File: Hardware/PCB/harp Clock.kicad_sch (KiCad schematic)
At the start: 16 parts, among them J2 AudioJack3_Ground_SwitchTR, J3 AudioJack3_Ground_SwitchTR, Q1 AO3401A, U1 74LVC1G157, U3 ADuM1201BR NOT NORMALLY STOCK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

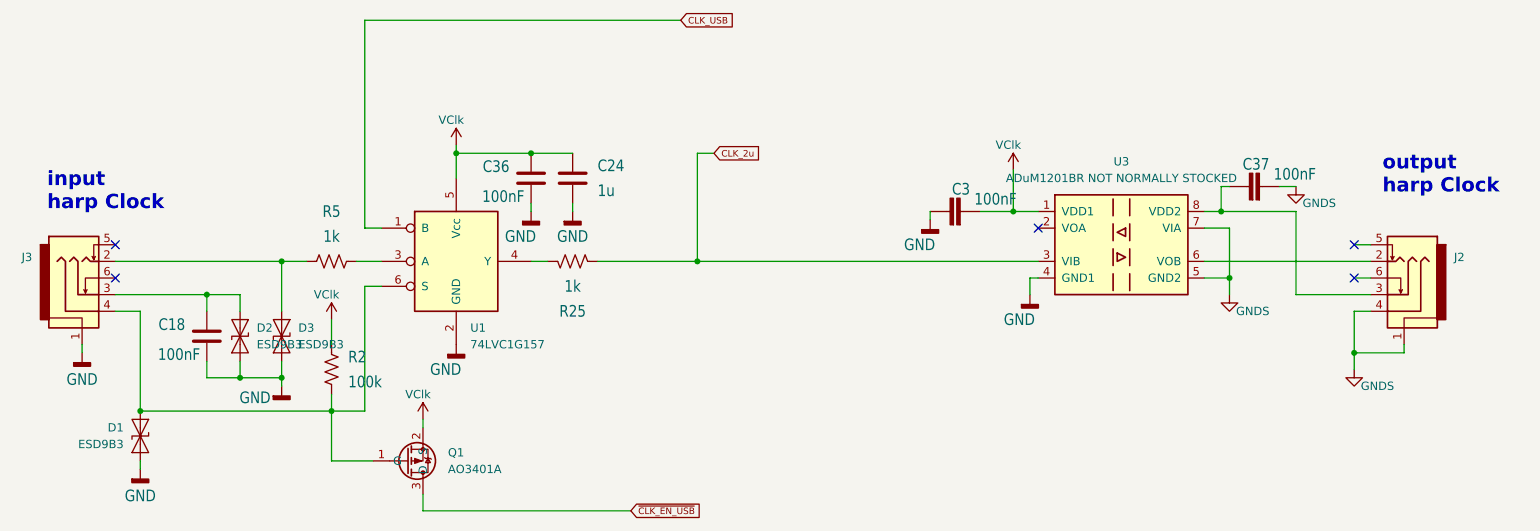
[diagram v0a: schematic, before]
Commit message: FastStepper DRC=0
DRC=0
ainda não revisto com mais ninguém
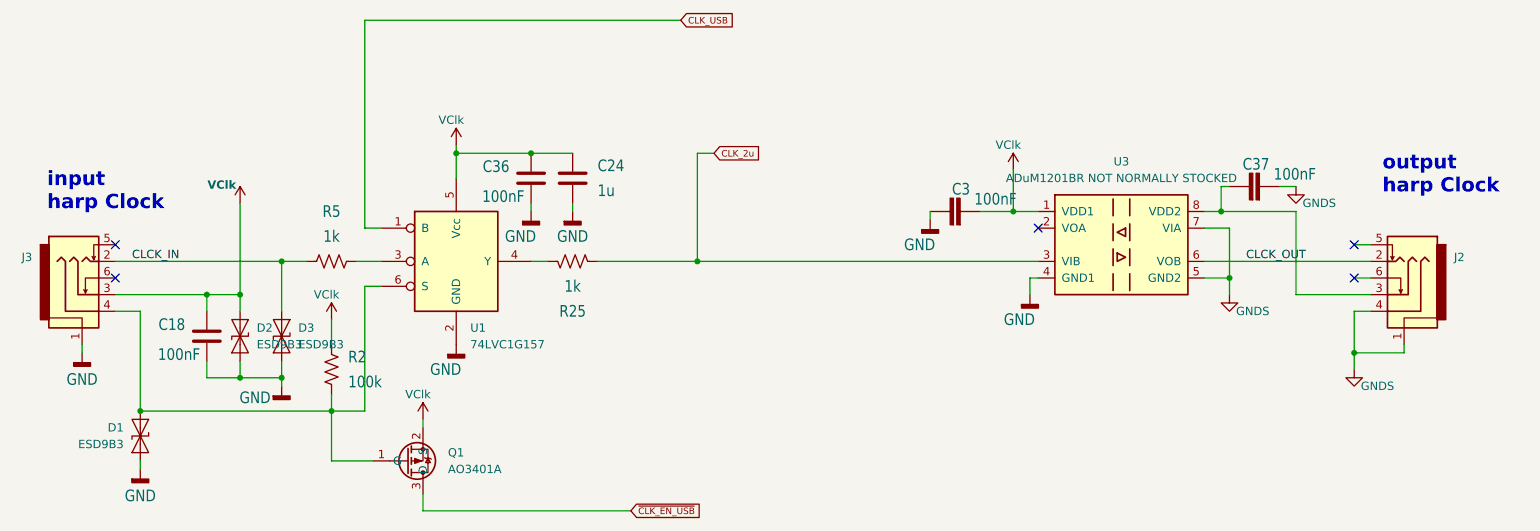
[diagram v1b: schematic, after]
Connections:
- net VClk: now also C18.2, D2.2 (A2), J3.3
- net CLCK_IN: now reaches D3.2 (A2), J3.2, R5.2
- net CLCK_OUT: now reaches J2.2, U3.6 (VOB)
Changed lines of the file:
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@@
+	)
+	(junction
+		(at 68.58 113.03)
+		(diameter 0)
+		(color 0 0 0 0)
 	)
 	(junction
@@
 	(wire
 		(pts
-			(xy 74.93 107.95) (xy 49.53 107.95)
-		)
-		(stroke
-			(width 0)
-			(type default)
-		)
-	)
-	(wire
-		(pts
 			(xy 53.34 139.7) (xy 53.34 138.43)
 		)
@@
 		(pts
 			(xy 90.17 107.95) (xy 86.36 107.95)
+		)
+		(stroke
+			(width 0)
+			(type default)
+		)
+	)
+	(wire
+		(pts
+			(xy 49.53 107.95) (xy 74.93 107.95)
 		)
 		(stroke
@@
 	(wire
 		(pts
+			(xy 68.58 99.06) (xy 68.58 113.03)
+		)
+		(stroke
+			(width 0)
+			(type default)
+		)
+	)
+	(wire
+		(pts
 			(xy 218.44 100.33) (xy 218.44 96.52)
 		)
@@
 			(width 0)
 			(type default)
+		)
+	)
+	(label "CLCK_OUT"
+		(at 222.25 107.95 0)
+		(effects
+			(font
+				(size 1.27 1.27)
+			)
+			(justify left bottom)
+		)
+	)
+	(label "CLCK_IN"
+		(at 52.07 107.95 0)
+		(effects
+			(font
+				(size 1.27 1.27)
+			)
+			(justify left bottom)
 		)
 	)
@@
 					(unit 1)
 				)
+			)
+		)
+	)
+	(symbol
+		(lib_id "FastStepper SymbLib:VClk")
+		(at 68.58 99.06 0)
+		(unit 1)
+		(exclude_from_sim no)
+		(in_bom yes)
+		(on_board yes)
+		(dnp no)
+		(property "Reference" "#PWR017"
+			(at 68.58 102.87 0)
+			(effects
+				(font
+					(size 1.27 1.27)
+				)
+				(hide yes)
+			)
+		)
+		(property "Value" "VClk"
+			(at 65.786 96.266 0)
+			(effects
+				(font
+					(size 1.27 1.27)
+					(thickness 0.254)
+					(bold yes)
+				)
+			)
+		)
+		(property "Footprint" ""
+			(at 68.58 99.06 0)
+			(effects
+				(font
+					(size 1.27 1.27)
+				)
+				(hide yes)
+			)
+		)
+		(property "Datasheet" ""
+			(at 68.58 99.06 0)
+			(effects
+				(font
+					(size 1.27 1.27)
+				)
+				(hide yes)
+			)
+		)
+		(property "Description" "Power symbol creates a global label with name \"VClk\""
+			(at 68.58 99.06 0)
+			(effects
+				(font
+					(size 1.27 1.27)
+				)
+				(hide yes)
+			)
+		)
+		(pin "1"
+		)
+		(instances
+			(project "FastStepper"
+				(path "/7345d9dc-7969-46b6-9229-988073b8033c/aad6949d-d213-4fed-8e5b-4ea13cc4c883"
+					(reference "#PWR017")
+					(unit 1)
+				)

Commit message: ver comentarios no .txt
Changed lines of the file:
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@@
 	)
 	(junction
+		(at 237.49 107.95)
+		(diameter 0)
+		(color 0 0 0 0)
+	)
+	(junction
 		(at 74.93 107.95)
 		(diameter 0)
@@
 	(wire
 		(pts
-			(xy 215.9 107.95) (xy 241.3 107.95)
+			(xy 215.9 107.95) (xy 237.49 107.95)
 		)
 		(stroke
@@
 	(wire
 		(pts
-			(xy 229.87 113.03) (xy 241.3 113.03)
+			(xy 223.52 113.03) (xy 241.3 113.03)
 		)
 		(stroke
@@
 	(wire
 		(pts
-			(xy 229.87 100.33) (xy 229.87 113.03)
+			(xy 223.52 100.33) (xy 223.52 113.03)
 		)
 		(stroke
@@
 	(wire
 		(pts
+			(xy 237.49 107.95) (xy 241.3 107.95)
+		)
+		(stroke
+			(width 0)
+			(type default)
+		)
+	)
+	(wire
+		(pts
 			(xy 74.93 125.73) (xy 74.93 123.19)
 		)
@@
 	(wire
 		(pts
-			(xy 218.44 100.33) (xy 229.87 100.33)
+			(xy 237.49 105.41) (xy 237.49 107.95)
+		)
+		(stroke
+			(width 0)
+			(type default)
+		)
+	)
+	(wire
+		(pts
+			(xy 218.44 100.33) (xy 223.52 100.33)
 		)
 		(stroke
@@
 		)
 	)
-	(label "CLCK_OUT"
-		(at 222.25 107.95 0)
-		(effects
-			(font
-				(size 1.27 1.27)
-			)
-			(justify left bottom)
-		)
-	)
 	(label "CLCK_IN"
 		(at 52.07 107.95 0)
@@
 		)
 	)
+	(global_label "CLCK_OUT"
+		(shape input)
+		(at 237.49 105.41 180)
+		(fields_autoplaced yes)
+		(effects
+			(font
+				(size 1.27 1.27)
+			)
+			(justify right)
+		)
+		(property "Intersheetrefs" "${INTERSHEET_REFS}"
+			(at 225.0705 105.41 0)
+			(effects
+				(font
+					(size 1.27 1.27)
+				)
+				(justify right)
+				(hide yes)
+			)
+		)
+	)
 	(global_label "CLK_2u"
 		(shape input)
@@
 			)
 		)
+		(property "OEPSPN" ""
+			(at 63.5 119.38 0)
+			(effects
+				(font
+					(size 1.27 1.27)
+				)
+				(hide yes)
+			)
+		)
 		(pin "1"
 		)
@@
 			)
 		)
+		(property "OEPSPN" ""
+			(at 68.58 119.38 90)
+			(effects
+				(font
+					(size 1.27 1.27)
+				)
+				(hide yes)
+			)
+		)
 		(pin "1"
 		)
@@
 			)
 		)
+		(property "OEPSPN" ""
+			(at 93.98 138.43 0)
+			(effects
+				(font
+					(size 1.27 1.27)
+				)
+				(hide yes)
+			)
+		)
 		(pin "3"
 		)
@@
 			)
 		)
+		(property "OEPSPN" ""
+			(at 53.34 134.62 90)
+			(effects
+				(font
+					(size 1.27 1.27)
+				)
+				(hide yes)
+			)
+		)
 		(pin "1"
 		)
@@
 			)
 		)
+		(property "OEPSPN" ""
+			(at 44.45 109.22 0)
+			(effects
+				(font
+					(size 1.27 1.27)
+				)
+				(hide yes)
+			)
+		)
 		(pin "1"
 		)
@@
 			)
 		)
+		(property "OEPSPN" ""
+			(at 119.38 107.95 90)
+			(effects
+				(font
+					(size 1.27 1.27)
+				)
+				(hide yes)
+			)
+		)
 		(pin "1"
 		)
@@
 			)
 		)
+		(property "OEPSPN" ""
+			(at 246.38 109.22 0)
+			(effects
+				(font
+					(size 1.27 1.27)
+				)
+				(hide yes)
+			)
+		)
 		(pin "1"
 		)
@@
 			)
 		)
+		(property "OEPSPN" ""
+			(at 82.55 107.95 90)
+			(effects
+				(font
+					(size 1.27 1.27)
+				)
+				(hide yes)
+			)
+		)
 		(pin "1"
 		)
@@
 			)
 		)
+		(property "OEPSPN" ""
+			(at 101.6 107.95 0)
+			(effects
+				(font
+					(size 1.27 1.27)
+				)
+				(hide yes)
+			)
+		)
 		(pin "6"
 		)
@@
 			)
 		)
+		(property "OEPSPN" ""
+			(at 203.2 105.41 0)
+			(effects
+				(font
+					(size 1.27 1.27)
+				)
+				(hide yes)
+			)
+		)
 		(pin "1"
 		)
@@
 			)
 		)
+		(property "OEPSPN" ""
+			(at 74.93 119.38 90)
+			(effects
+				(font
+					(size 1.27 1.27)
+				)
+				(hide yes)
+			)
+		)
 		(pin "1"
 		)
@@
 			)
 		)
+		(property "OEPSPN" ""
+			(at 113.03 95.25 0)
+			(effects
+				(font
+					(size 1.27 1.27)
+				)
+				(hide yes)
+			)
+		)
 		(pin "1"
 		)
@@
 			)
 		)
+		(property "OEPSPN" ""
+			(at 82.55 124.46 0)
+			(effects
+				(font
+					(size 1.27 1.27)
+				)
+				(hide yes)
+			)
+		)
 		(pin "1"
 		)
@@
 			)
 		)
+		(property "OEPSPN" ""
+			(at 119.38 95.25 0)
+			(effects
+				(font
+					(size 1.27 1.27)
+				)
+				(hide yes)
+			)
+		)
 		(pin "2"
 		)
@@
 			)
 		)
+		(property "OEPSPN" ""
+			(at 222.25 96.52 90)
+			(effects
+				(font
+					(size 1.27 1.27)
+				)
+				(hide yes)
+			)
+		)
 		(pin "1"
 		)
@@
 				(hide yes)
 			)
+		)
+		(property "OEPSPN" ""
+			(at 176.53 100.33 90)
+			(effects
+				(font
+					(size 1.27 1.27)
+				)
+				(hide yes)
+			)

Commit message: MPN & OEPSPN adicionados; ainda em falta novos PNs a ser emitidos
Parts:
- C18, C3, C36, C37: MPN C1005X7R1H104K050BB -> CGA2B3X7R1H104K050BB; OEPS OEPS010004 -> (none); OEPSPN (none) -> OEPS010016
- C24: MPN ?!?!? a case?? -> CL10A105KA8NNNC; OEPS TBD ?? -> (none); OEPSPN (none) -> OEPS010022
- D1, D2, D3: MPN (none) -> TBD ESD9B3
- J2, J3: MPN PJ-316A-6A -> TBD AliExpress? PJ-316A-6A
- Q1: MPN (none) -> TBD AO3401A
- R2: MPN TBD -> ERJ-2RKF1003X; OEPS OEPS?? -> (none); OEPSPN (none) -> OEPS020019
- R25, R5: MPN TBD -> ERJ-2RKF1001X; OEPS OEPS?? -> (none); OEPSPN (none) -> OEPS020006
- U1: MPN 74LVC1G157GV -> TBD 74LVC1G157GV
- U3: MPN (none) -> TBD q MPN?
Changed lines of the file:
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@@
 			)
 		)
-		(property "MPN" "C1005X7R1H104K050BB"
+		(property "MPN" "CGA2B3X7R1H104K050BB"
 			(at 63.5 119.38 0)
 			(effects
@@
 			)
 		)
-		(property "OEPS" "OEPS010004"
-			(at 63.5 119.38 0)
-			(effects
-				(font
-					(size 1.27 1.27)
-				)
-				(justify left bottom)
-				(hide yes)
-			)
-		)
-		(property "OEPSPN" ""
+		(property "OEPSPN" "OEPS010016"
 			(at 63.5 119.38 0)
 			(effects
@@
 			)
 		)
+		(property "MPN" "TBD ESD9B3"
+			(at 68.58 119.38 90)
+			(effects
+				(font
+					(size 1.27 1.27)
+				)
+				(hide yes)
+			)
+		)
 		(pin "1"
 		)
@@
 			)
 		)
+		(property "MPN" "TBD AO3401A"
+			(at 93.98 138.43 0)
+			(effects
+				(font
+					(size 1.27 1.27)
+				)
+				(hide yes)
+			)
+		)
 		(pin "3"
 		)
@@
 			)
 		)
+		(property "MPN" "TBD ESD9B3"
+			(at 53.34 134.62 90)
+			(effects
+				(font
+					(size 1.27 1.27)
+				)
+				(hide yes)
+			)
+		)
 		(pin "1"
 		)
@@
 			)
 		)
-		(property "MPN" "PJ-316A-6A"
+		(property "MPN" "TBD AliExpress? PJ-316A-6A"
 			(at 44.45 109.22 0)
 			(effects
@@
 			)
 		)
-		(property "MPN" "TBD"
+		(property "MPN" "ERJ-2RKF1001X"
 			(at 119.38 107.95 0)
 			(effects
@@
 			)
 		)
-		(property "OEPS" "OEPS??"
-			(at 119.38 107.95 0)
-			(effects
-				(font
-					(size 1.27 1.27)
-				)
-				(justify left bottom)
-				(hide yes)
-			)
-		)
-		(property "OEPSPN" ""
+		(property "OEPSPN" "OEPS020006"
 			(at 119.38 107.95 90)
 			(effects
@@
 			)
 		)
-		(property "MPN" "PJ-316A-6A"
+		(property "MPN" "TBD AliExpress? PJ-316A-6A"
 			(at 246.38 109.22 0)
 			(effects
@@
 			)
 		)
-		(property "MPN" "TBD"
+		(property "MPN" "ERJ-2RKF1001X"
 			(at 82.55 107.95 0)
 			(effects
@@
 			)
 		)
-		(property "OEPS" "OEPS??"
-			(at 82.55 107.95 0)
-			(effects
-				(font
-					(size 1.27 1.27)
-				)
-				(justify left bottom)
-				(hide yes)
-			)
-		)
-		(property "OEPSPN" ""
+		(property "OEPSPN" "OEPS020006"
 			(at 82.55 107.95 90)
 			(effects
@@
 			)
 		)
-		(property "MPN" "74LVC1G157GV"
+		(property "MPN" "TBD 74LVC1G157GV"
 			(at 101.6 107.95 0)
 			(effects
@@
 			)
 		)
+		(property "MPN" "TBD q MPN? "
+			(at 203.2 105.41 0)
+			(effects
+				(font
+					(size 1.27 1.27)
+				)
+				(hide yes)
+			)
+		)
 		(pin "1"
 		)
@@
 			)
 		)
+		(property "MPN" "TBD ESD9B3"
+			(at 74.93 119.38 90)
+			(effects
+				(font
+					(size 1.27 1.27)
+				)
+				(hide yes)
+			)
+		)
 		(pin "1"
 		)
@@
 			)
 		)
-		(property "MPN" "C1005X7R1H104K050BB"
+		(property "MPN" "CGA2B3X7R1H104K050BB"
 			(at 113.03 95.25 0)
 			(effects
@@
 			)
 		)
-		(property "OEPS" "OEPS010004"
-			(at 113.03 95.25 0)
-			(effects
-				(font
-					(size 1.27 1.27)
-				)
-				(justify left bottom)
-				(hide yes)
-			)
-		)
-		(property "OEPSPN" ""
+		(property "OEPSPN" "OEPS010016"
 			(at 113.03 95.25 0)
 			(effects
@@
 			)
 		)
-		(property "MPN" "TBD"
+		(property "MPN" "ERJ-2RKF1003X"
 			(at 82.55 124.46 0)
 			(effects
@@
 			)
 		)
-		(property "OEPS" "OEPS??"
-			(at 82.55 124.46 0)
-			(effects
-				(font
-					(size 1.27 1.27)
-				)
-				(justify left bottom)
-				(hide yes)
-			)
-		)
-		(property "OEPSPN" ""
+		(property "OEPSPN" "OEPS020019"
 			(at 82.55 124.46 0)
 			(effects
@@
 			)
 		)
-		(property "MPN" "?!?!? a case??"
+		(property "MPN" "CL10A105KA8NNNC"
 			(at 119.38 95.25 0)
 			(effects
@@
 			)
 		)
-		(property "OEPS" "TBD ??"
-			(at 119.38 95.25 0)
-			(effects
-				(font
-					(size 1.27 1.27)
-				)
-				(justify left bottom)
-				(hide yes)
-			)
-		)
-		(property "OEPSPN" ""
+		(property "OEPSPN" "OEPS010022"
 			(at 119.38 95.25 0)
 			(effects
@@
 			)
 		)
-		(property "MPN" "C1005X7R1H104K050BB"
+		(property "MPN" "CGA2B3X7R1H104K050BB"
 			(at 222.25 96.52 0)
 			(effects
@@
 			)
 		)
-		(property "OEPS" "OEPS010004"
-			(at 222.25 96.52 0)
-			(effects
-				(font
-					(size 1.27 1.27)
-				)
-				(justify left bottom)
-				(hide yes)
-			)
-		)
-		(property "OEPSPN" ""
+		(property "OEPSPN" "OEPS010016"
 			(at 222.25 96.52 90)
 			(effects
@@
 			)
 		)
-		(property "MPN" "C1005X7R1H104K050BB"
+		(property "MPN" "CGA2B3X7R1H104K050BB"
 			(at 176.53 100.33 0)
 			(effects
@@
 			)
 		)
-		(property "OEPS" "OEPS010004"
-			(at 176.53 100.33 0)
-			(effects
-				(font
-					(size 1.27 1.27)
-				)
-				(justify left bottom)
-				(hide yes)
-			)
-		)
-		(property "OEPSPN" ""
+		(property "OEPSPN" "OEPS010016"
 			(at 176.53 100.33 90)
 			(effects

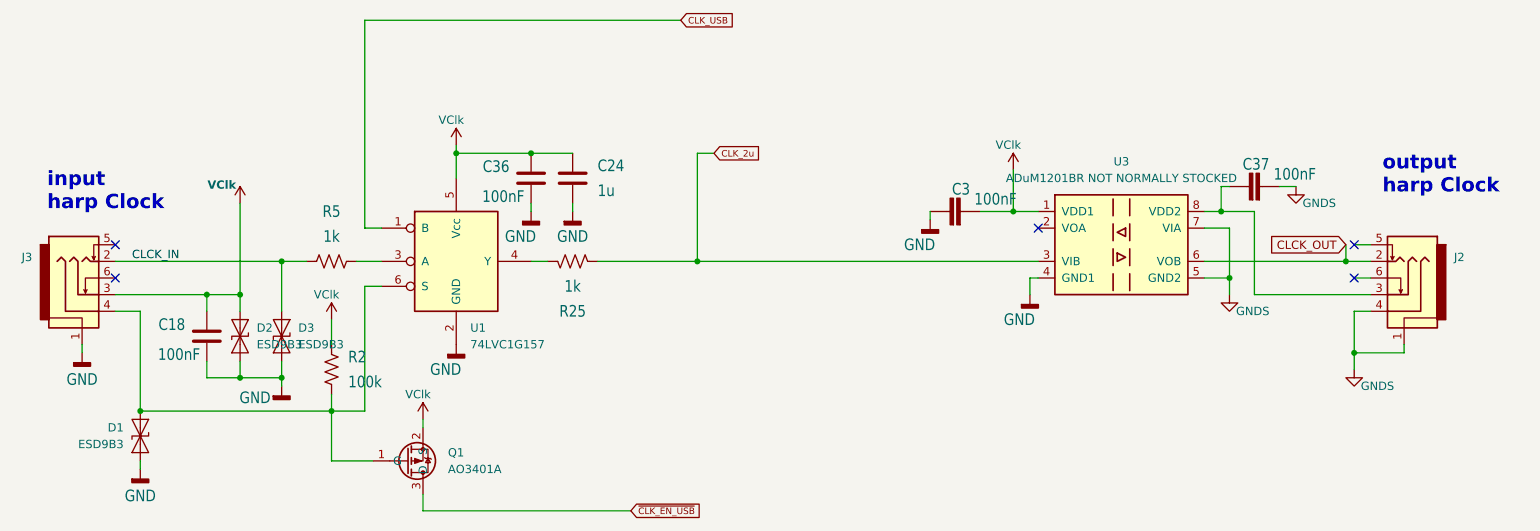
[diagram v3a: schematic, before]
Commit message: MPN & OEPSPN concluded
concluded but not yet certified
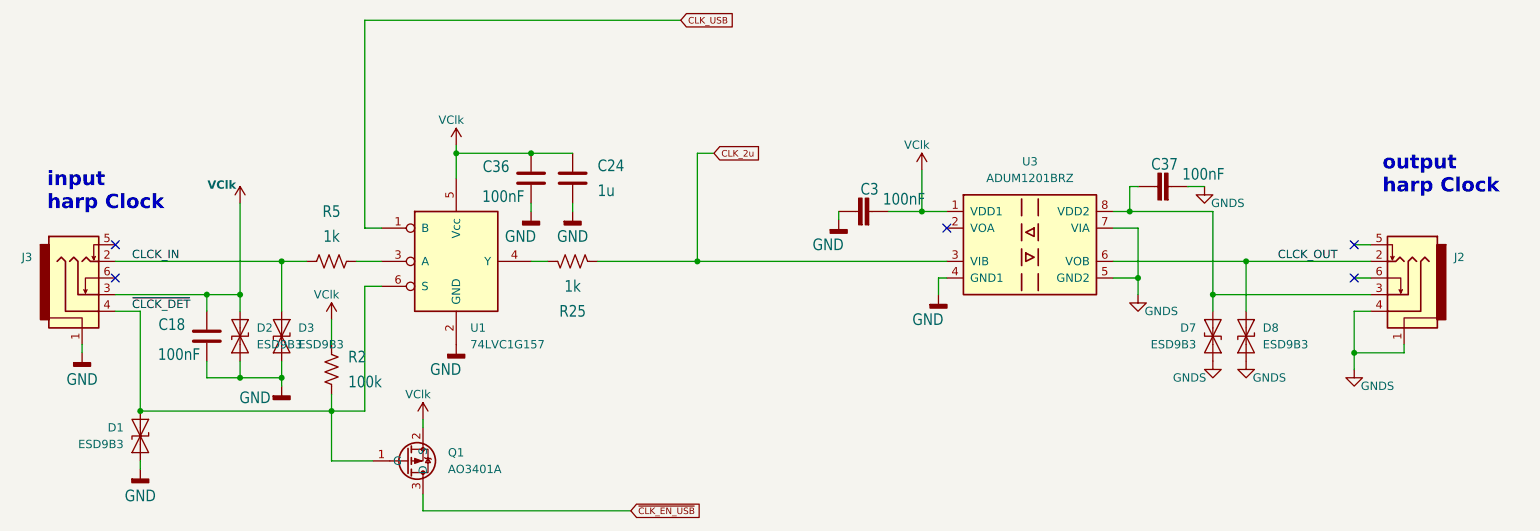
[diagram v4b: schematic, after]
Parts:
- added D7, D8: ESD9B3, Diode_SMD:D_SOD-923, symbol Diode:ESD9B3.3ST5G
- D1, D2, D3: MPN TBD ESD9B3 -> ESD9B3.3ST5G; OEPSPN (none) -> OEPS030039
- J2, J3: value AudioJack3_Ground_SwitchTR -> PJ-316A-6A; footprint Connector_Audio:Jack_3.5mm_PJ311_Horizontal -> FastStepper PCBLib:Jack_3.5mm_PJ316A_Horizontal; MPN TBD AliExpress? PJ-316A-6A -> LCSC Electronics PJ-316A-6A; OEPSPN (none) -> OEPS070129
- Q1: MPN TBD AO3401A -> AO3401A; OEPSPN (none) -> OEPS060021
- U1: MPN TBD 74LVC1G157GV -> 74LVC1G157GV,125; OEPSPN (none) -> OEPS080170
- U3: value ADuM1201BR NOT NORMALLY STOCKED -> ADUM1201BRZ; MPN TBD q MPN? -> ADUM1201BRZ; OEPSPN (none) -> OEPS080172
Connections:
- net CLCK_OUT: now also D8.2 (A2)
- net GNDS: now also D7.1 (A1), D8.1 (A1)
- net ~{CLCK_DET}: now reaches D1.2 (A2), J3.4, Q1.1 (G), R2.2, U1.6 (S)
- net at C37.1, J2.3, U3.8 (VDD2): now also D7.2 (A2)
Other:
- moved on the sheet: C3, C37, U3
